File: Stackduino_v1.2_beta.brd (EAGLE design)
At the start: 86.4 x 62.9 mm, 30 parts, among them IC2 7805T, U1 ATMEGA328P_PDIP

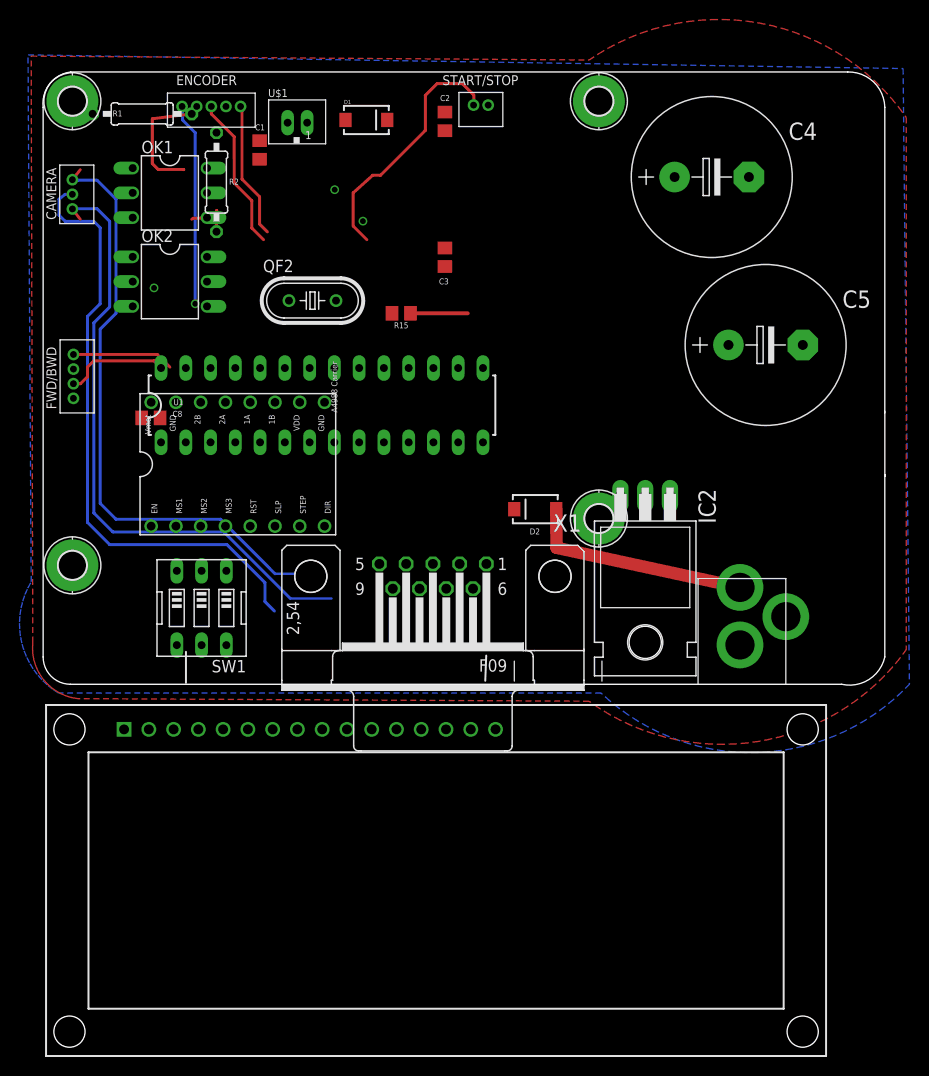
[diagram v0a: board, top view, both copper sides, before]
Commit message: corrected error in component list
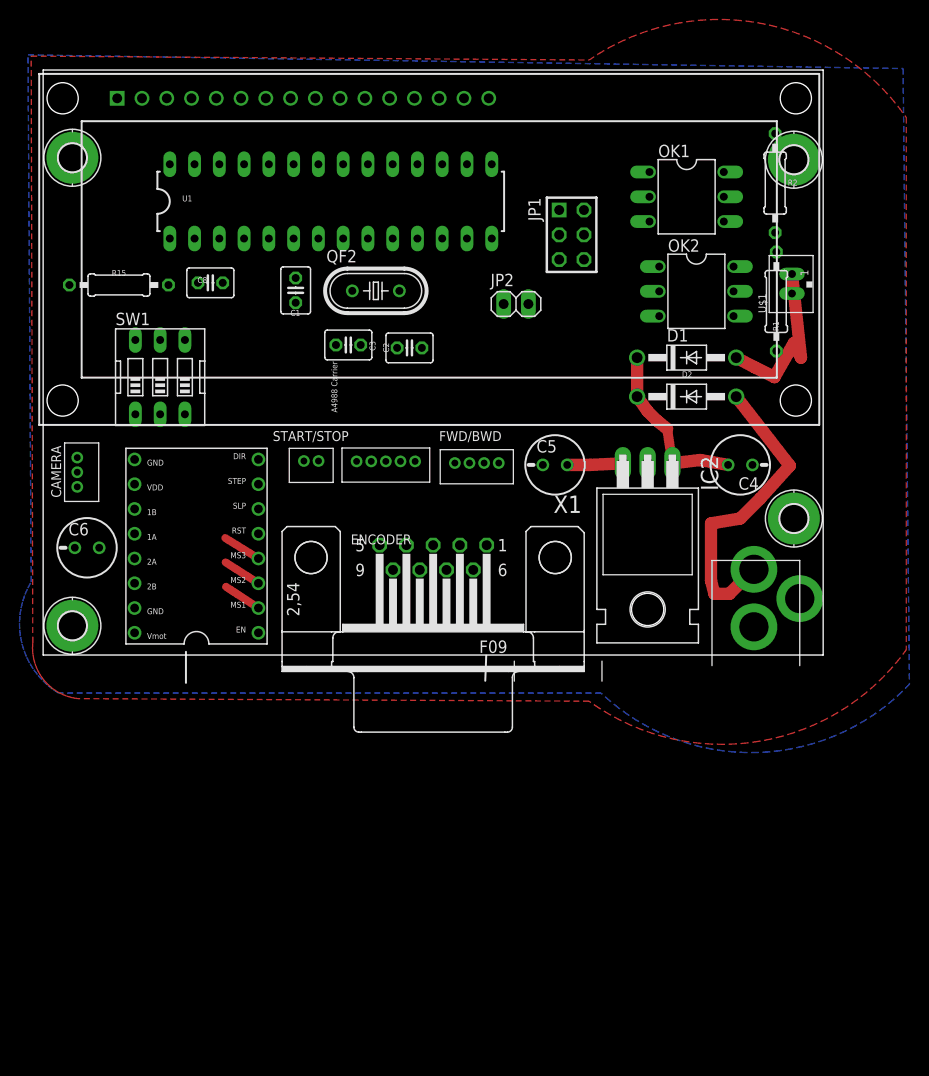
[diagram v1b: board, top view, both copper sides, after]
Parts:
- added C6: (no value), rcl:SANYO-OSCON_C
- added JP1: AVR-5_AVR-ISP-6, Stackduino-SMD:AVR-5_AVR-ISP-6
- added JP2: (no value), pinhead:1X02
- C1, C2, C3, C8: device eagle-ltspice:C0805 -> rcl:C025-030X050
- C4, C5: device rcl:E7,5-16 -> rcl:SANYO-OSCON_C
- D1, D2: device SparkFun-DiscreteSemi:SMA-DIODE -> diode:DO41-10
- R1, R2: device resistor:0207/10 -> rcl:0207/10
- R15: device eagle-ltspice:R0805 -> rcl:0207/10
- moved R1 67.8 mm to (75.2, 51.3), turned to 270 degrees
- moved U$2 64.7 mm to (39.6, 56.6)
- moved R2 57.3 mm to (75.1, 63.4)
- moved OK2 54.0 mm to (67.0, 52.3)
- moved U$1 53.5 mm to (76.8, 53.0), turned to 90 degrees
- moved OK1 53.0 mm to (66.0, 62.0)
- moved D1 40.9 mm to (66.0, 45.5)
- moved ENCODER 40.6 mm to (35.1, 34.9)
- moved START/STOP 40.4 mm to (25.8, 35.6)
- moved FWD/BWD 39.1 mm to (40.7, 36.0), turned to 0 degrees
- moved C4 29.7 mm to (71.5, 34.5), turned to 180 degrees
- moved R15 29.1 mm to (7.78, 53.0), turned to 180 degrees
- moved CAMERA 28.5 mm to (3.50, 33.8)
- moved C5 24.9 mm to (52.5, 34.5)
- moved SW1 24.1 mm to (12.0, 43.5), turned to 0 degrees
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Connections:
- removed net +5V: C5.+, IC2.3
- removed net A: U$2.15
- removed net K: U$2.16
- removed net N$1 (its old number): C8.1, R15.1, U1.1
- removed net N$12: C4.+, D1.C, D2.C, IC2.1
- removed net N$14: A4988_CARRIER.VMOT
- removed net VCC1: A4988_CARRIER.VDD
- removed net VDD: U$2.2
- removed net VSS: U$2.1
- new net MCU_MISO: JP1.1, U1.18
- new net MCU_MOSI: JP1.4, U1.17
- new net MCU_RESET: C8.1, JP1.5, R15.1, U1.1
- new net MCU_SCK: JP1.3, U1.19
- new net N$4: 12VDC.TIP, D2.A
- net GND: now also C6.-, JP1.6, U$2.1, U$2.16, U$2.5
- net MCU_RX: now also JP2.1
- net MCU_TX: now also JP2.2
- net VCC: now also A4988_CARRIER.VDD, C5.+, IC2.3, JP1.2, U$2.15, U$2.2
- net VIN: now also A4988_CARRIER.VMOT, C4.+, C6.+, D1.C, D2.C, IC2.1; no longer 12VDC.TIP, D2.A
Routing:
- net OPT1: track 64.3 -> 0.00 mm
- net OPT2: track 63.0 -> 0.00 mm
- net CAM_GND: track 62.8 -> 0.00 mm
- net N$4: track 0.00 -> 31.8 mm
- net START_STOP: track 26.0 -> 0.00 mm
- net ENC_SWITCH: track 20.8 -> 0.00 mm, vias 1 -> 0
- net N$1: track 0.00 -> 18.7 mm
- net ENC_B: track 15.9 -> 0.00 mm
- net ENC_A: track 14.0 -> 0.00 mm
- net N$36: track 12.2 -> 0.00 mm
- net FWD: track 11.2 -> 0.00 mm
- net BWD: track 10.8 -> 0.00 mm
- net VIN: track 23.2 -> 17.9 mm
- net N$34: track 5.22 -> 0.00 mm
- net MS3: track 0.00 -> 4.00 mm
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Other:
- board size 86.4 x 62.9 mm -> 80 x 60 mm
